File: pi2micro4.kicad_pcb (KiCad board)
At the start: 2 copper layers, 17 parts, among them M1 microduino_base, M2 microduino_base, M3 microduino_base, M4 microduino_base, P1 CONN_13X2, U1 NCP1117ST33T3G, U2 txs0104e

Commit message: nuevo buffer
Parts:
- added K1: CONN_3, SIL-3, F.Cu at (151.1, 144.8)
- added K2: CONN_3, SIL-3, F.Cu at (141.6, 144.8)
- added R3: 1k, SMD-0603, B.Cu at (149.9, 112.4)
- added R4: 1k, SMD-0603, B.Cu at (138.4, 94.0)
- added R5: 1k, SMD-0603, B.Cu at (138.4, 97.8)
- added R6: 1k, SMD-0603, B.Cu at (138.4, 95.9)
- added U3: txs0104e, TSSOP-14, B.Cu at (143.5, 114.3)
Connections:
- P1 pad 15: /Rp_GPIO -> (no net)
- P1 pad 19: (no net) -> /Rp_MOSI
- P1 pad 21: (no net) -> /Rp_MISO
- P1 pad 23: (no net) -> /Rp_SCLK
- P1 pad 3: (no net) -> /Rp_SDA
- P1 pad 5: (no net) -> /Rp_SCL
- U2 pad 10: /Rp_GPIO -> /Rp_SCL
- U2 pad 11: /Rp_RST -> /Rp_SDA
- U2 pad 4: /RST -> /A4
- U2 pad 5: /D2 -> /A5
- U2 pad 8: (no net) -> Net-(K2-Pad2)
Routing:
- net /3V3_RB: track 18.3 -> 115.0 mm, vias 1 -> 2
- net Net-(K2-Pad2): track 0.00 -> 83.5 mm, vias 0 -> 1
- net GND: track 254.0 -> 305.6 mm, vias 2 -> 0
- net Net-(K1-Pad2): track 0.00 -> 40.6 mm
- net /A5: track 69.2 -> 99.6 mm
- net /D8: track 114.8 -> 139.2 mm
- net /Rp_RST: track 14.4 -> 37.7 mm
- net /Rp_SCL: track 0.00 -> 21.6 mm, vias 0 -> 1
- net /RX0: track 84.7 -> 105.8 mm, vias 0 -> 1
- net /Rp_SDA: track 0.00 -> 21.0 mm
- net /D3: track 113.4 -> 95.8 mm
- net /Rp_GPIO: track 16.6 -> 0.00 mm
- net /Rp_MOSI: track 0.00 -> 16.3 mm, vias 0 -> 1
- net /Rp_MISO: track 0.00 -> 15.1 mm, vias 0 -> 1
- net /RST: track 198.4 -> 183.4 mm
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
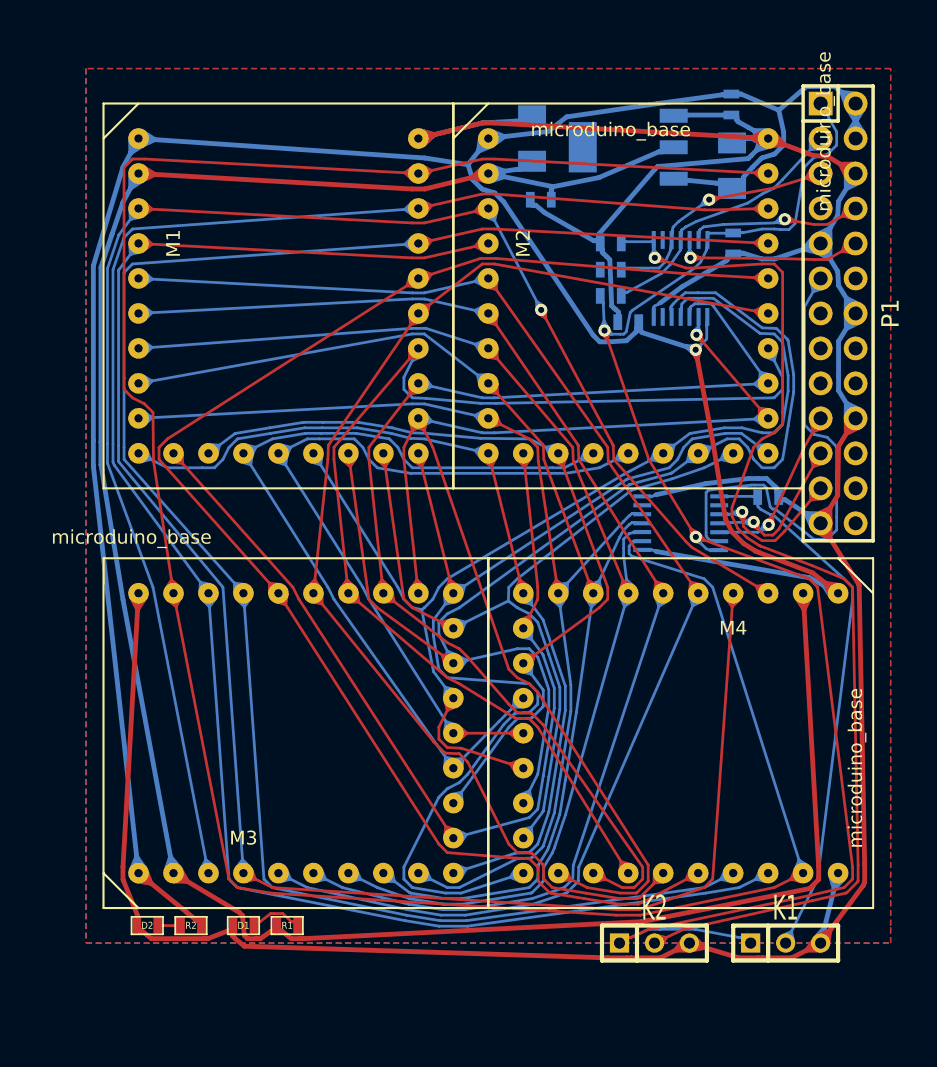
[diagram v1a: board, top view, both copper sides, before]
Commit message: corregido el footprint del microduino
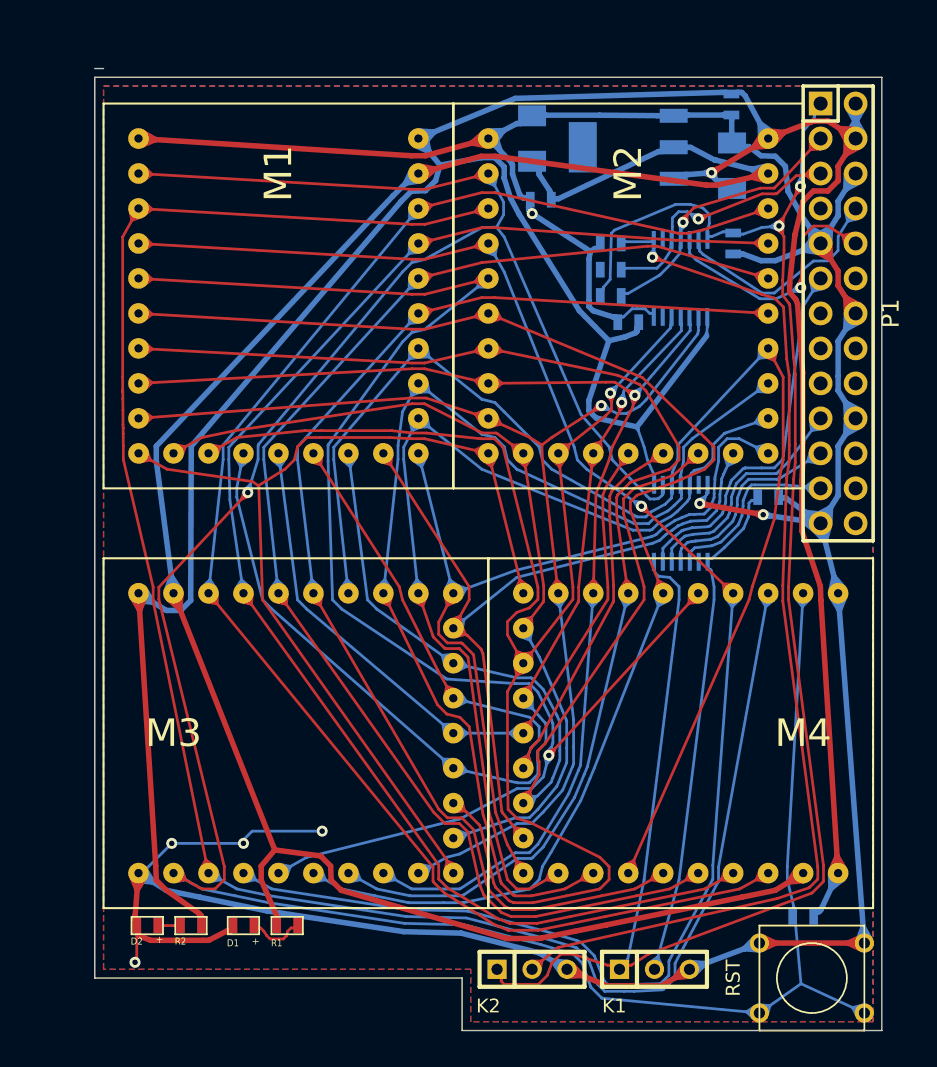
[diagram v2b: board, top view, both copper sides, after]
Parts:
- added R7: 1k, SMD-0603, B.Cu at (152.4, 142.9)
- added SW1: RST, SW_PUSH_SMALL, F.Cu at (153.0, 147.3)
- M1, M2, M3, M4: footprint microduino_base -> Microduino:microduino_base
- moved K1 9.71 mm to (141.6, 146.7)
- moved K2 9.09 mm to (132.7, 146.7)
- turned U3 to 0 degrees
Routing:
- net +5V: track 220.7 -> 257.1 mm
- net /RST: track 183.4 -> 215.9 mm, vias 0 -> 1
- net /3V3_RB: track 115.0 -> 141.9 mm
- net /D8: track 139.2 -> 113.6 mm
- net /A5: track 99.6 -> 118.7 mm, vias 0 -> 1
- net +3.3V: track 183.5 -> 166.8 mm
- net /D3: track 95.8 -> 108.7 mm
- net /D4: track 114.0 -> 125.0 mm, vias 0 -> 1
- net /RX0: track 105.8 -> 95.2 mm
- net /A0: track 77.0 -> 66.6 mm
- net /Rp_RST: track 37.7 -> 28.3 mm
- net /A7: track 87.0 -> 78.1 mm
- net /A1: track 67.7 -> 75.7 mm
- net /TX1: track 94.8 -> 102.6 mm, vias 0 -> 1
- net /D5: track 138.6 -> 131.0 mm, vias 0 -> 1
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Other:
- board outline added: 57.2 x 69.8 mm
- net class Default: via_dia 0.889 -> 0.8; via_drill 0.635 -> 0.4
- rule trace_min: 0.254 -> 0.2
- rule via_min_drill: 0.508 -> 0.4
- rule via_min_size: 0.889 -> 0.8
- board text added: "+"

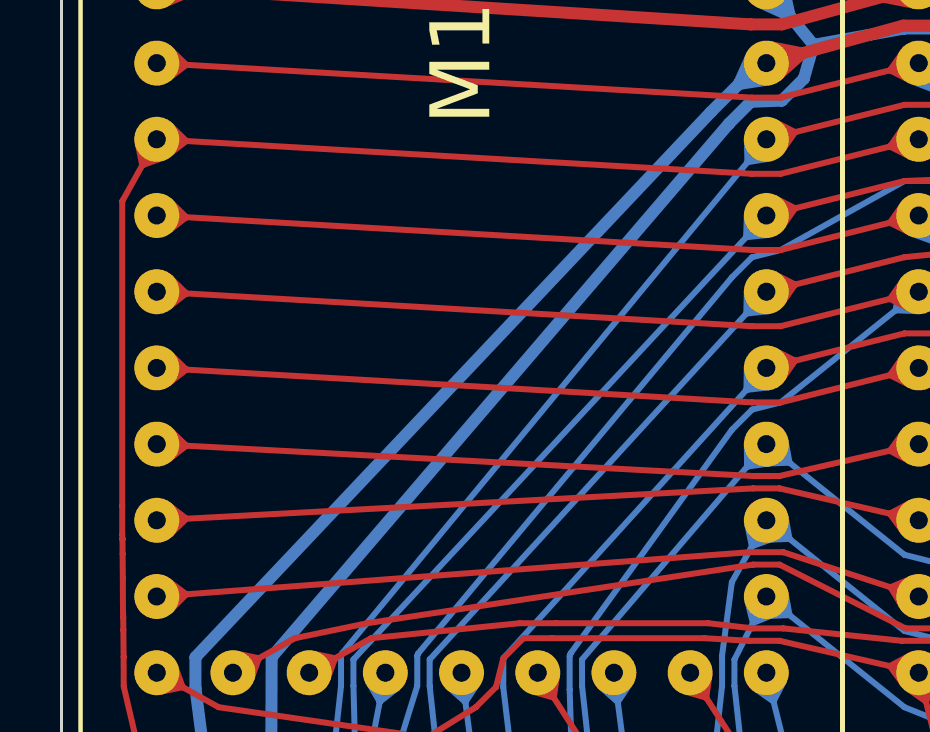
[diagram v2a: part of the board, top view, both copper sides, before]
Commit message: logo de hackbo para kicad
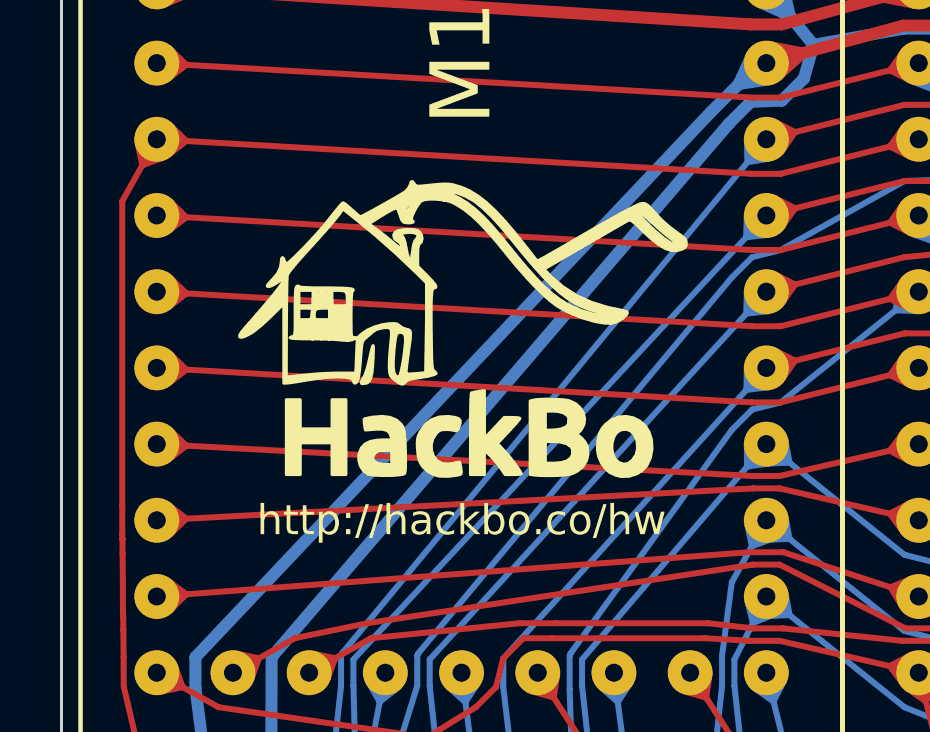
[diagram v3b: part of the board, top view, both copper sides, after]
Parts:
- added G***: LOGO, Logos:hackbo, F.Cu at (114.3, 99.1)
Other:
- board text added: "http://hackbo.co/hw"

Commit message: logo de openhardware
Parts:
- added G***: LOGO, Logos:oshw, F.Cu at (116.8, 128.9)
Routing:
- net GND: track 312.3 -> 317.1 mm

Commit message: labels
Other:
- board text added: "pi2micro4 V1.0 HackBo 2014 @unjuguetero Designed in Colombia"

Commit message: previsualizaciones
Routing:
- net GND: track 317.1 -> 316.1 mm
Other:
- board size 57.2 x 69.8 mm -> 57.2 x 69.2 mm
- board text added: "3.3V"
- board text added: "5V"
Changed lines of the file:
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@@
     (area 97.095095 73.35 173.1 151.393501)
     (thickness 1.6)
-    (drawings 13)
-    (tracks 1813)
+    (drawings 14)
+    (tracks 1812)
     (zones 0)
     (modules 28)
@@
     (visible_elements FFFFFFFF)
     (pcbplotparams
-      (layerselection 271613953)
+      (layerselection 284983297)
       (usegerberextensions true)
       (excludeedgelayer true)
@@
       (xy 5.842 -1.234683) (xy 5.842 -1.234683)) (layer F.SilkS) (width 0.1))
   )
+  (gr_text 3.3V (at 111.76 146.05) (layer F.SilkS)
+    (effects (font (size 1 1) (thickness 0.25)))
+  )
+  (gr_text 5V (at 104.14 146.05) (layer F.SilkS)
+    (effects (font (size 1 1) (thickness 0.25)))
+  )
   (gr_text "pi2micro4 V1.0\nHackBo 2014\n@unjuguetero\nDesigned in Colombia\n" (at 145.415 135.255) (layer F.SilkS)
     (effects (font (size 0.7 0.7) (thickness 0.125)) (justify right))
@@
     (effects (font (size 0.508 0.508) (thickness 0.127)))
   )
-  (gr_line (start 101.6 81.28) (end 100.965 81.28) (angle 90) (layer Edge.Cuts) (width 0.1))
   (dimension 55.88 (width 0.3) (layer Cmts.User)
     (gr_text "55,880 mm" (at 129.54 74.85) (layer Cmts.User)
@@
     (arrow2b (pts (xy 165.1 83.82) (xy 165.686421 84.946504)))
   )
+  (segment (start 103.886 146.177) (end 103.759 146.177) (width 0.2) (layer B.Cu) (net 0))
   (segment (start 154.8625 138.4724) (end 154.4335 139.4855) (width 0.4) (layer F.Cu) (net 1))
   (segment (start 154.8625 138.4724) (end 155.4155 139.4235) (width 0.4) (layer F.Cu) (net 1))
@@
   (segment (start 132.588 91.6742) (end 132.7253 91.8115) (width 0.2) (layer B.Cu) (net 27))
   (segment (start 132.588 90.805) (end 132.588 91.6742) (width 0.2) (layer B.Cu) (net 27))
-  (segment (start 104.013 146.05) (end 103.886 146.177) (width 0.2) (layer F.Cu) (net 27))
-  (via (at 103.886 146.177) (size 0.8) (layers F.Cu B.Cu) (net 27))
-  (segment (start 103.886 146.177) (end 103.759 146.177) (width 0.2) (layer B.Cu) (net 27))
-  (segment (start 104.013 143.51) (end 104.013 146.05) (width 0.2) (layer F.Cu) (net 27))
   (segment (start 104.14 139.7) (end 104.394 139.7) (width 0.2) (layer B.Cu) (net 27))
   (segment (start 104.042 140.9261) (end 104.6108 139.9844) (width 0.4) (layer F.Cu) (net 27))
@@
   (segment (start 111.76 137.287) (end 112.395 136.652) (width 0.2) (layer B.Cu) (net 27))
   (segment (start 117.475 136.652) (end 117.475 132.715) (width 0.2) (layer B.Cu) (net 27))
+  (via (at 102.235 143.51) (size 0.8) (layers F.Cu B.Cu) (net 27))
+  (segment (start 104.013 143.51) (end 102.235 143.51) (width 0.2) (layer F.Cu) (net 27))
   (segment (start 112.522 143.51) (end 112.7395 143.6815) (width 0.2) (layer F.Cu) (net 28))
   (segment (start 112.7395 143.6815) (end 112.8395 143.6815) (width 0.2) (layer F.Cu) (net 28))

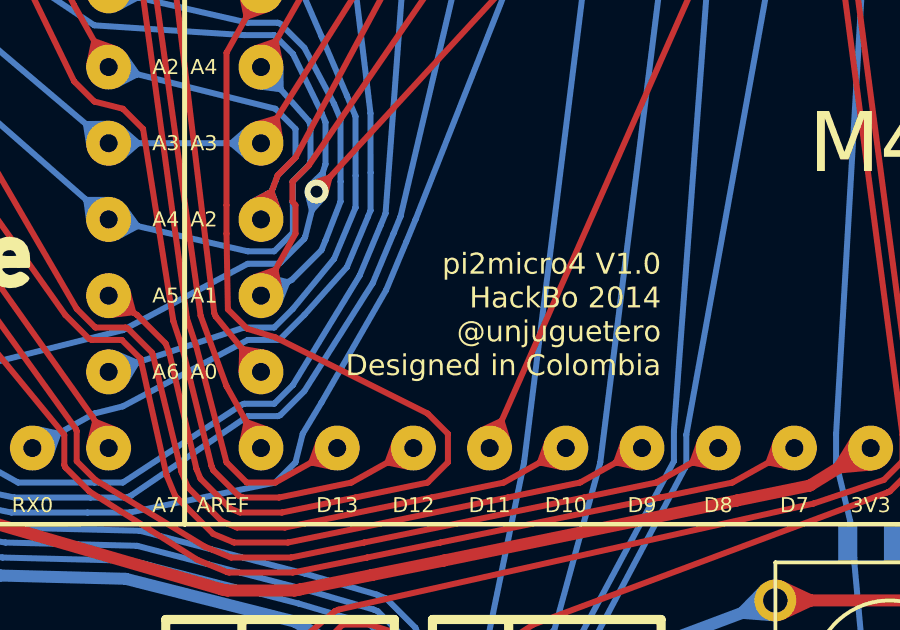
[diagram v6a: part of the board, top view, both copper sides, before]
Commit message: add usb dimmension
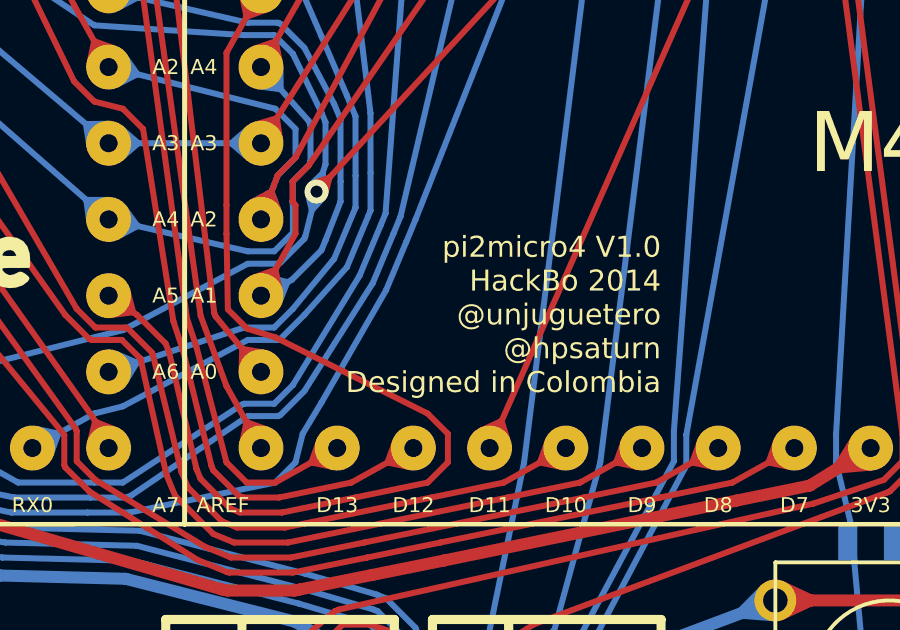
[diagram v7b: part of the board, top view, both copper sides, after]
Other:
- board text added: "pi2micro4 V1.0 HackBo 2014 @unjuguetero @hpsaturn Designed in Colombia"
- board text removed: "pi2micro4 V1.0 HackBo 2014 @unjuguetero Designed in Colombia"

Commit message: guias
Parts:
- added MH1: MountingHole_3mm_RevA_Date21Jun2010, Mounting_Holes:MountingHole_3mm, F.Cu at (119.4, 86.4)
- added MH2: MountingHole_3mm_RevA_Date21Jun2010, Mounting_Holes:MountingHole_3mm, F.Cu at (134.6, 104.1)
- added MH3: MountingHole_3mm_RevA_Date21Jun2010, Mounting_Holes:MountingHole_3mm, F.Cu at (118.7, 132.1)
- moved G2 26.0 mm to (142.9, 128.9)
- moved G1 1.27 mm to (113.0, 99.1)
- moved D1 0.64 mm to (111.1, 143.5)
- moved D2 0.64 mm to (104.1, 143.5)
- moved M3 0.64 mm to (126.4, 129.5)
- moved R1 0.64 mm to (114.3, 143.5)
- moved R2 0.64 mm to (107.3, 143.5)
- moved M1 0.63 mm to (113.7, 109.2)
- renumbered G*** to G1, G*** to G2
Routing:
- net GND: track 316.1 -> 451.3 mm, vias 7 -> 19
- net /3V3_RB: track 141.9 -> 98.7 mm
- net /A5: track 118.7 -> 82.8 mm
- net /RST: track 215.9 -> 188.2 mm, vias 1 -> 2
- net Net-(K2-Pad2): track 81.4 -> 103.2 mm
- net /D7: track 121.0 -> 136.1 mm
- net /D8: track 113.6 -> 128.6 mm
- net /D6: track 149.6 -> 162.4 mm
- net /RX0: track 95.2 -> 107.2 mm, vias 1 -> 0
- net /A0: track 66.6 -> 77.7 mm
- net /AREF: track 70.7 -> 81.7 mm
- net /A1: track 75.7 -> 86.7 mm
- net /D4: track 125.0 -> 135.9 mm, vias 1 -> 0
- net /Rp_SCLK: track 14.6 -> 25.0 mm
- net +3.3V: track 166.8 -> 156.8 mm, vias 0 -> 1
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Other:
- board size 57.2 x 69.2 mm -> 57.8 x 69.8 mm
